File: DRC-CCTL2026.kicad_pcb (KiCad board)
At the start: 2 copper layers, 80 x 60 mm, 75 parts, among them J1 USB, J10 SW3, J12 LCD_BackLight, J2 FDCAN1, J3 FDCAN2, J4 FDCAN3, J5 SW1, J6 SW2, J7 STLINK, J8 I2C, J9 USART, Q1 MMBT3904, SW1 RESET, SW2 DIP, U1 STM32G474RETx, U2 AZ1084C-3.3, U3 74AHC1G125, Y1 8M10PB/XT324-10/80

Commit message: CANの終端抵抗を削除、シルクスクリーンを調整
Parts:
- removed JP1, JP2, JP3: TR, Connector_PinHeader_2.54mm:PinHeader_1x02_P2.54mm_Vertical
- moved R7 4.92 mm to (127.0, 85.0), turned to 90 degrees
- moved R8 4.92 mm to (127.0, 97.5), turned to 90 degrees
- moved R9 4.92 mm to (127.0, 110.0), turned to 90 degrees
- moved G*** 3.48 mm to (131.7, 113.7)
- renumbered D6 to D2, D2 to D3, D3 to D4, D4 to D5, D5 to D6, R9 to R10, R10 to R11, R11 to R3, R3 to R4, R4 to R5, R5 to R6, R6 to R7, R7 to R8, R8 to R9
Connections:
- R7 pad 1: Net-(JP1-B) -> /FDCAN1/FDCAN_H
- R8 pad 1: Net-(JP2-B) -> /FDCAN2/FDCAN_H
- R9 pad 1: Net-(JP3-B) -> /FDCAN3/FDCAN_H
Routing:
- net /FDCAN3/FDCAN_L: track 6.84 -> 12.5 mm
- net /FDCAN2/FDCAN_L: track 6.79 -> 12.4 mm
- net /FDCAN1/FDCAN_L: track 6.75 -> 12.1 mm
- net Net-(JP3-B): track 3.65 -> 0.00 mm
- net Net-(JP2-B): track 3.65 -> 0.00 mm
- net Net-(JP1-B): track 3.65 -> 0.00 mm
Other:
- board text added: "DRC-CCTL2026 v0.1.0"
- board text removed: "DRC-CCTL2026 v0.0.2"

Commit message: v0.2.0
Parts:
- removed the C1 at (139.2, 91.9)
- removed the C10 at (145.6, 89.4)
- removed the C11 at (150.1, 99.5)
- removed the C12 at (151.7, 99.5)
- removed the C2 at (134.2, 99.5)
- removed the C3 at (183.7, 102.1)
- removed the C6 at (142.0, 84.3)
- removed the C7 at (144.3, 98.2)
- removed the C8 at (153.2, 99.5)
- removed the C9 at (154.4, 90.6)
- removed the D1 at (176.0, 84.2)
- removed the J1 at (175.3, 73.0)
- removed J12: LCD_BackLight, Connector_JST:JST_XH_B2B-XH-A_1x02_P2.50mm_Vertical
- removed the R1 at (176.6, 72.7)
- removed R5: 1k, Resistor_SMD:R_0603_1608Metric_Pad0.98x0.95mm_HandSolder
- removed the R6 at (125.2, 123.7)
- removed the SW1 at (183.7, 102.1)
- removed the U1 at (149.4, 94.4)
- removed Y1: 8M10PB/XT324-10/80, lib:8M10PB_XT324-10_80
- added C17: 0.1u, Capacitor_SMD:C_0603_1608Metric_Pad1.08x0.95mm_HandSolder, B.Cu at (154.4, 95.7)
- added C18: 0.1u, Capacitor_SMD:C_0603_1608Metric_Pad1.08x0.95mm_HandSolder, B.Cu at (149.4, 88.1)
- added C19: 0.1u, Capacitor_SMD:C_0603_1608Metric_Pad1.08x0.95mm_HandSolder, B.Cu at (141.8, 93.2)
- added C20: 1u, Capacitor_SMD:C_0603_1608Metric_Pad1.08x0.95mm_HandSolder, B.Cu at (150.6, 95.7)
- added C21: 0.1u, Capacitor_SMD:C_0603_1608Metric_Pad1.08x0.95mm_HandSolder, B.Cu at (151.9, 97.0)
- added C22: 1u, Capacitor_SMD:C_0603_1608Metric_Pad1.08x0.95mm_HandSolder, B.Cu at (154.4, 99.5)
- added C23: 0.1u, Capacitor_SMD:C_0603_1608Metric_Pad1.08x0.95mm_HandSolder, B.Cu at (153.2, 98.2)
- added C24: 1u, Capacitor_SMD:C_0603_1608Metric_Pad1.08x0.95mm_HandSolder, B.Cu at (140.5, 95.7)
- added C25: 0.1u, Capacitor_SMD:C_0603_1608Metric_Pad1.08x0.95mm_HandSolder, B.Cu at (124.0, 124.9)
- added D10: SS2040FL, Diode_SMD:D_SOD-123F, B.Cu at (127.8, 80.5)
- added D11: SS2040FL, Diode_SMD:D_SOD-123F, B.Cu at (143.0, 80.5)
- added D3: SS2040FL, Diode_SMD:D_SOD-123F, B.Cu at (177.3, 100.8)
- added D7: LED2, LED_SMD:LED_0603_1608Metric_Pad1.05x0.95mm_HandSolder, F.Cu at (120.8, 98.2)
- added D8: LED3, LED_SMD:LED_0603_1608Metric_Pad1.05x0.95mm_HandSolder, F.Cu at (120.8, 85.5)
- added J10: USB_C, Connector_USB:USB_C_Receptacle_GCT_USB4105-xx-A_16P_TopMnt_Horizontal, F.Cu at (127.8, 73.5)
- added J11: USB_C, Connector_USB:USB_C_Receptacle_GCT_USB4105-xx-A_16P_TopMnt_Horizontal, F.Cu at (143.0, 73.5)
- added R12: 5.1k, Resistor_SMD:R_0603_1608Metric_Pad0.98x0.95mm_HandSolder, B.Cu at (129.1, 74.5)
- added R13: 5.1k, Resistor_SMD:R_0603_1608Metric_Pad0.98x0.95mm_HandSolder, B.Cu at (126.5, 74.5)
- added R14: 5.1k, Resistor_SMD:R_0603_1608Metric_Pad0.98x0.95mm_HandSolder, B.Cu at (144.3, 74.1)
- added R15: 5.1k, Resistor_SMD:R_0603_1608Metric_Pad0.98x0.95mm_HandSolder, B.Cu at (141.8, 74.1)
- added R16: 4.7k, Resistor_SMD:R_0603_1608Metric_Pad0.98x0.95mm_HandSolder, B.Cu at (178.6, 91.9)
- added R17: 4.7k, Resistor_SMD:R_0603_1608Metric_Pad0.98x0.95mm_HandSolder, B.Cu at (178.6, 97.0)
- added R18: 4.7k, Resistor_SMD:R_0603_1608Metric_Pad0.98x0.95mm_HandSolder, B.Cu at (178.6, 107.1)
- added R19: 4.7k, Resistor_SMD:R_0603_1608Metric_Pad0.98x0.95mm_HandSolder, B.Cu at (178.6, 112.2)
- added R3: 1k, Resistor_SMD:R_0603_1608Metric_Pad0.98x0.95mm_HandSolder, F.Cu at (118.9, 120.5)
- added R4: 1k, Resistor_SMD:R_0603_1608Metric_Pad0.98x0.95mm_HandSolder, F.Cu at (118.9, 122.4)
- added SW2: SS-12D00G3, lib:SS-12D00G3, F.Cu at (130.3, 124.9)
- added SW3: SW_Push, Button_Switch_SMD:SW_SPST_EVQPE1, F.Cu at (124.0, 124.9)
- added U2: CH340E, Package_SO:MSOP-10_3x3mm_P0.5mm, F.Cu at (120.2, 75.4)
- added U4: STM32G474RETx, Package_QFP:LQFP-64_10x10mm_P0.5mm, F.Cu at (148.1, 94.4)
- C13, C16: value 1u -> 0.1u
- C15: value 0.1u -> 4.7u; footprint Capacitor_SMD:C_0603_1608Metric_Pad1.08x0.95mm_HandSolder -> Capacitor_SMD:C_0805_2012Metric_Pad1.18x1.45mm_HandSolder; moved to F.Cu
- C3: renamed from C17; moved to F.Cu
- C4: renamed from C18; moved to F.Cu
- C5: renamed from C19; moved to F.Cu
- C6: renamed from C20; moved to F.Cu
- C7: renamed from C21; moved to F.Cu
- C8: renamed from C22; moved to F.Cu
- CAN1: renamed from FDCAN1; footprint footprints:SOIC127P600X175-8N -> lib:SO8_SOT96-1_NXP; moved to F.Cu
- CAN2: renamed from FDCAN2; footprint footprints:SOIC127P600X175-8N -> lib:SO8_SOT96-1_NXP; moved to F.Cu
- CAN3: renamed from FDCAN3; footprint footprints:SOIC127P600X175-8N -> lib:SO8_SOT96-1_NXP; moved to F.Cu
- D2: value 1N4148W -> SS2040FL; footprint Diode_SMD:D_SOD-123 -> Diode_SMD:D_SOD-123F
- D4: value RGB -> SS2040FL; footprint LED_SMD:LED_WS2812B_PLCC4_5.0x5.0mm_P3.2mm -> Diode_SMD:D_SOD-123F; moved to B.Cu
- D5: value 5V -> 1N4148W; footprint LED_SMD:LED_0603_1608Metric_Pad1.05x0.95mm_HandSolder -> Diode_SMD:D_SOD-123; moved to B.Cu
- D6: value LED -> LED1
- G***: moved to B.Cu
- J1: renamed from J7; footprint Connector_JST:JST_PH_S6B-PH-K_1x06_P2.00mm_Horizontal -> Connector_IDC:IDC-Header_2x03_P2.54mm_Vertical
- J8: value I2C -> I2C1
- J9: value USART -> I2C2; footprint Connector_JST:JST_XH_S4B-XH-A_1x04_P2.50mm_Horizontal -> Connector_JST:JST_XH_S5B-XH-A_1x05_P2.50mm_Horizontal
- Q1: moved to F.Cu
- R1: renamed from R4; value 470 -> 1k; moved to F.Cu
- R2: value 5.1k -> 1k; moved to F.Cu
- R6: renamed from R3; moved to F.Cu
- U3: value 74AHC1G125 -> CH340E; footprint Package_TO_SOT_SMD:SOT-353_SC-70-5 -> Package_SO:MSOP-10_3x3mm_P0.5mm
- moved D5 74.8 mm to (177.3, 77.9), turned to 180 degrees
- moved R2 71.7 mm to (118.9, 118.6), turned to 180 degrees
- moved D1 67.5 mm to (167.2, 75.4), turned to -90 degrees
- moved R1 67.4 mm to (169.7, 75.4)
- moved SW1 58.6 mm to (127.8, 113.5), turned to 90 degrees
- moved J7 51.5 mm to (186.2, 86.8)
- moved J6 50.9 mm to (178.6, 86.8)
- moved J1 50.6 mm to (159.5, 74.1), turned to -90 degrees
- moved J5 50.3 mm to (171.0, 86.8)
- moved J9 49.9 mm to (181.5, 118.5), turned to 90 degrees
- moved C14 49.1 mm to (120.2, 74.1)
- moved D4 46.6 mm to (177.3, 116.0), turned to 180 degrees
- moved U3 44.5 mm to (135.4, 75.4), turned to 90 degrees
- moved G*** 34.0 mm to (165.3, 108.5), turned to 180 degrees
- moved C13 31.8 mm to (135.4, 74.1), turned to -90 degrees
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- renumbered C4 to C1, C24 to C10, C25 to C11, C26 to C12, C5 to C2, C23 to C9, D3 to D1, J10 to J7, SW2 to SW1, U2 to U1
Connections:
- net /LCD_SCL renamed /LCD/LCD_SCL
- net /LCD_SDA renamed /LCD/LCD_SDA
- C13 pad 1: +3V3 -> GND
- C13 pad 2: GND -> +3V3
- C14 pad 2: +5V -> +3V3
- CAN1 pad 1: /FDCAN1_TX -> /FDCAN1/FDCAN_TX
- CAN1 pad 4: /FDCAN1_RX -> /FDCAN1/FDCAN_RX
- CAN2 pad 1: /FDCAN2_TX -> /FDCAN2/FDCAN_TX
- CAN2 pad 4: /FDCAN2_RX -> /FDCAN2/FDCAN_RX
- CAN3 pad 1: /FDCAN3_TX -> /FDCAN3/FDCAN_TX
- CAN3 pad 4: /FDCAN3_RX -> /FDCAN3/FDCAN_RX
- D2 pad 1: +3V3 -> +5V
- D2 pad 2: Net-(BZ1--) -> Net-(D2-A)
- D4 pad 1: +5V -> Net-(D4-K)
- D4 pad 2: unconnected-(D4-DOUT-Pad2) -> +3V3
- D5 pad 1: GND -> +3V3
- D5 pad 2: Net-(D5-A) -> Net-(BZ1--)
- J1 pad 2: +5V -> Net-(D2-A)
- J1 pad 3: unconnected-(J7-Pin_3-Pad3) -> +3V3
- J5 pad 2: /SW1 -> /STM32G474/SW1
- J6 pad 2: /SW2 -> /STM32G474/SW2
- J7 pad 2: /SW3 -> /STM32G474/SW3
- J8 pad 2: +3V3 -> Net-(D3-K)
- J8 pad 3: /I2C_INT -> /STM32G474/I2C1_INT
- J8 pad 4: /I2C_SCL -> /STM32G474/I2C1_SCL
- J8 pad 5: /I2C_SDA -> /STM32G474/I2C1_SDA
- J9 pad 2: +3V3 -> Net-(D4-K)
- J9 pad 3: /USART_TX -> /STM32G474/I2C2_INT
- J9 pad 4: /USART_RX -> /STM32G474/I2C2_SCL
- LCD1 pad A: +3V3 -> Net-(SW2-B)
- R2 pad 1: Net-(J1-CC2) -> /STM32G474/LED1
- R2 pad 2: GND -> Net-(D6-A)
- R6 pad 1: /BUZZER -> /STM32G474/BZ_TIM1_CH4
- SW1 pad 1: /DIP1 -> /STM32G474/DIP1
- SW1 pad 2: /DIP2 -> /STM32G474/DIP2
- SW1 pad 3: /DIP3 -> /STM32G474/DIP3
- SW1 pad 4: /DIP4 -> /STM32G474/DIP4
- U3 pad 1: GND -> /USBC2/USB_D_P
- U3 pad 2: /RGB -> /USBC2/USB_D_N
- U3 pad 4: Net-(D4-DIN) -> unconnected-(U3-~{RTS}-Pad4)
- U3 pad 5: +5V -> unconnected-(U3-~{CTS}-Pad5)
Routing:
- net +3V3: track 325.8 -> 402.9 mm, vias 17 -> 16
- net /STM32G474/I2C1_INT: track 0.00 -> 65.0 mm
- net +5V: track 195.5 -> 130.8 mm, vias 7 -> 1
- net /LED_BI: track 56.8 -> 0.00 mm, vias 1 -> 0
- net /FDCAN3_RX: track 50.5 -> 0.00 mm, vias 2 -> 0
- net /BUZZER: track 50.3 -> 0.00 mm, vias 1 -> 0
- net /STM32G474/I2C2_INT: track 0.00 -> 48.5 mm
- net /FDCAN1_RX: track 46.4 -> 0.00 mm, vias 1 -> 0
- net Net-(D8-A): track 0.00 -> 45.9 mm, vias 0 -> 2
- net /STM32G474/I2C2_SCL: track 0.00 -> 45.3 mm
- net /I2C_SDA: track 45.3 -> 0.00 mm, vias 1 -> 0
- net /LCD/LCD_SCL: track 41.6 -> 86.0 mm
- net /FDCAN3_TX: track 44.4 -> 0.00 mm, vias 1 -> 0
- net /STM32G474/I2C2_SDA: track 0.00 -> 43.9 mm
- net /FDCAN2_RX: track 41.6 -> 0.00 mm, vias 1 -> 0
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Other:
- board text added: "1"
- board text added: "2"
- board text added: "3"
- board text added: "DRC-CCTL2026 v0.2.0"
- board text added: "Designed by kotek, March 2026"
- board text added: "FDCAN"
- board text added: "NRST"
- board text removed: "(SWO)"
- board text removed: "- 16x2 Char LCD - Piezo Buzzer - Full Color LED"
- board text removed: "- CAN FD x3 - USB x1 - I2C x1"
- board text removed: "- Switch x3"
- board text removed: "Created by kotek, March 2026"
- board text removed: "DRC-CCTL2026 v0.1.0"
- board text removed: "Features"
- board text removed: "LCD BackLight"
- board text removed: "Not for Programming"
- board text removed: "RST"
- board text removed: "RX"
- board text removed: "TX"

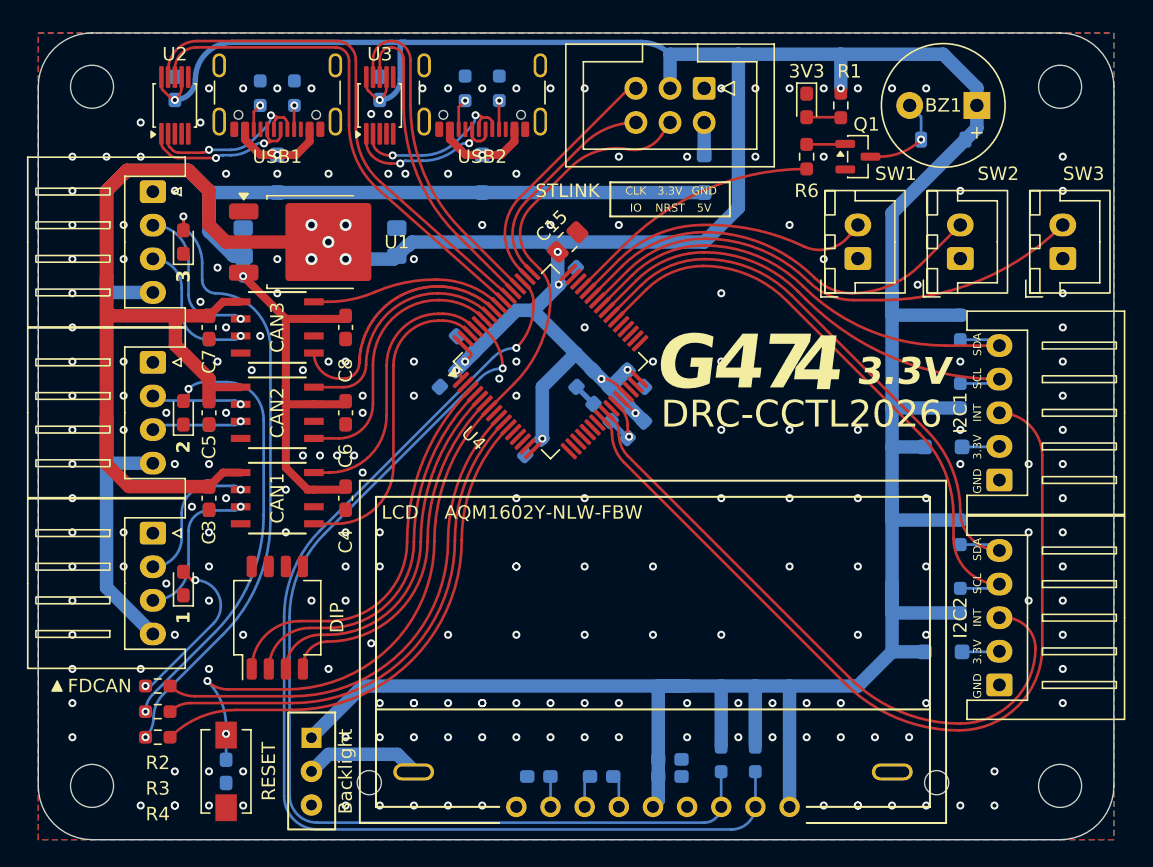
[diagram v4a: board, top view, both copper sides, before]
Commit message: v0.2.1, USB CDC に対応
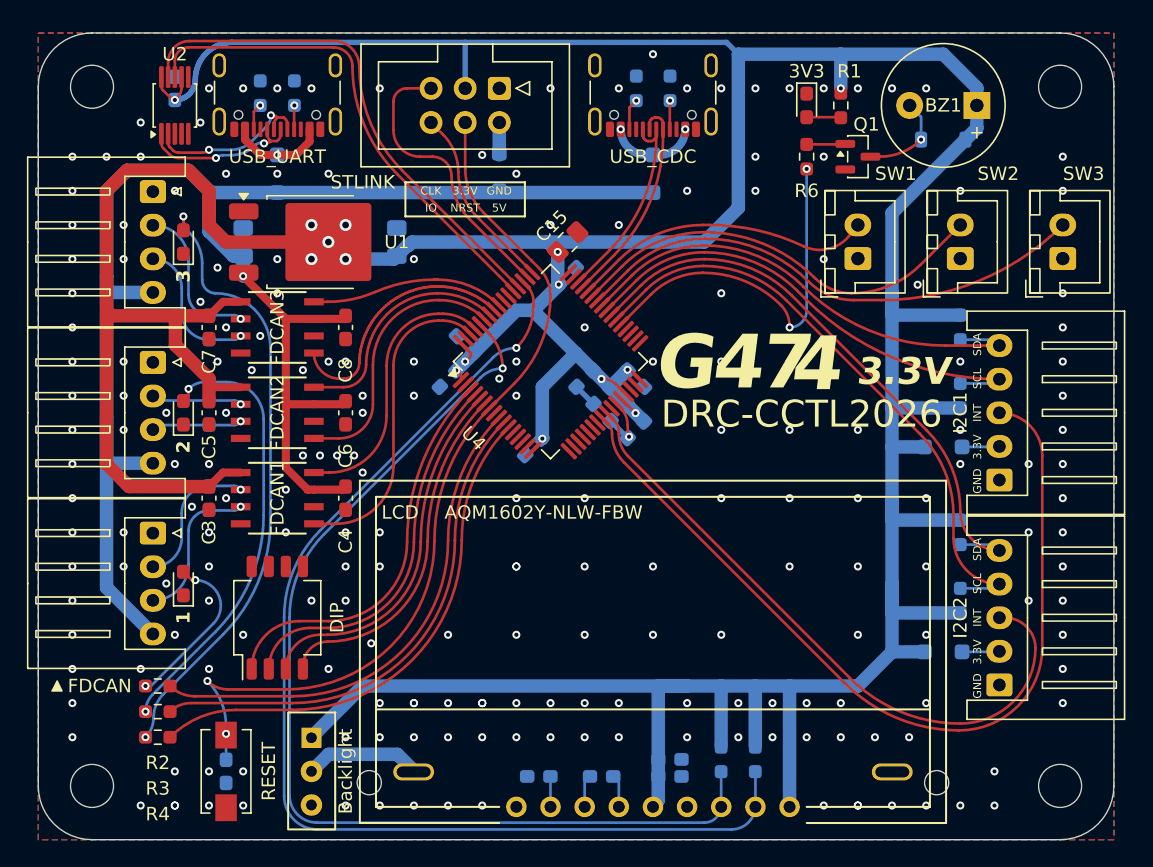
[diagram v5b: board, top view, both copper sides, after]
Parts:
- removed C14: 0.1u, Capacitor_SMD:C_0603_1608Metric_Pad1.08x0.95mm_HandSolder
- removed D11: SS2040FL, Diode_SMD:D_SOD-123F
- removed J11: USB_C, Connector_USB:USB_C_Receptacle_GCT_USB4105-xx-A_16P_TopMnt_Horizontal
- removed R14, R15: 5.1k, Resistor_SMD:R_0603_1608Metric_Pad0.98x0.95mm_HandSolder
- removed U3: CH340E, Package_SO:MSOP-10_3x3mm_P0.5mm
- added D9: SS2040FL, Diode_SMD:D_SOD-123F, B.Cu at (155.7, 80.5)
- added J12: USB_C, Connector_USB:USB_C_Receptacle_GCT_USB4105-xx-A_16P_TopMnt_Horizontal, F.Cu at (155.7, 73.5)
- added R20: 5.1k, Resistor_SMD:R_0603_1608Metric_Pad0.98x0.95mm_HandSolder, B.Cu at (154.5, 74.1)
- added R5: 5.1k, Resistor_SMD:R_0603_1608Metric_Pad0.98x0.95mm_HandSolder, B.Cu at (157.0, 74.1)
- moved D2 15.2 mm to (144.3, 80.3)
- moved C13 15.2 mm to (120.2, 74.1)
- moved J1 15.2 mm to (144.3, 74.1)
- moved G*** 12.2 mm to (155.7, 116.1)
- moved REF** 0.73 mm to (166.1, 116.3)
- renumbered CAN1 to FDCAN1, CAN2 to FDCAN2, CAN3 to FDCAN3
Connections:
- net /USBC1/USB_D_N renamed /USB_UART/USB_D_N
- net /USBC1/USB_D_P renamed /USB_UART/USB_D_P
- R6 pad 1: /STM32G474/BZ_TIM1_CH4 -> /STM32G474/BZ_TIM15_CH2
- U2 pad 8: /STM32G474/UART_USB1_RX -> /STM32G474/USART_USB_RX
- U2 pad 9: /STM32G474/UART_USB1_TX -> /STM32G474/USART_USB_TX
- U4 pad 37: unconnected-(U4-PB15-Pad37) -> /STM32G474/BZ_TIM15_CH2
- U4 pad 45: /STM32G474/BZ_TIM1_CH4 -> /STM32G474/USB_CDC_DM
- U4 pad 46: unconnected-(U4-PA12-Pad46) -> /STM32G474/USB_CDC_DP
- U4 pad 52: /STM32G474/USART_USB2_TX -> /STM32G474/USART_USB_TX
- U4 pad 53: /STM32G474/USART_USB2_RX -> /STM32G474/USART_USB_RX
- U4 pad 54: /STM32G474/UART_USB1_TX -> unconnected-(U4-PC12-Pad54)
- U4 pad 55: /STM32G474/UART_USB1_RX -> unconnected-(U4-PD2-Pad55)
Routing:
- net /STM32G474/UART_USB1_TX: track 38.7 -> 0.00 mm
- net /STM32G474/USART_USB_TX: track 0.00 -> 37.9 mm
- net /STM32G474/UART_USB1_RX: track 37.6 -> 0.00 mm
- net /STM32G474/USART_USB_RX: track 0.00 -> 36.8 mm
- net /STM32G474/BZ_TIM15_CH2: track 0.00 -> 28.1 mm, vias 0 -> 2
- net /STM32G474/USART_USB2_TX: track 25.1 -> 0.00 mm
- net /STM32G474/USART_USB2_RX: track 24.0 -> 0.00 mm
- net /STM32G474/BZ_TIM1_CH4: track 19.3 -> 0.00 mm
- net /STM32G474/USB_CDC_DM: track 0.00 -> 15.9 mm
- net /STM32G474/USB_CDC_DP: track 0.00 -> 15.5 mm
- net /USBC2/USB_D_N: track 13.0 -> 0.00 mm, vias 2 -> 0
- net /USBC2/USB_D_P: track 13.0 -> 0.00 mm, vias 2 -> 0
- net +3V3: track 402.9 -> 394.6 mm, vias 16 -> 15
- net Net-(D11-A): track 7.34 -> 0.00 mm, vias 1 -> 0
- net Net-(D9-A): track 0.00 -> 6.82 mm, vias 0 -> 2
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
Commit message: JLCPCB用に書き出し2
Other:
- board text removed: "4"
- board text removed: "7"
- board text removed: "G"
